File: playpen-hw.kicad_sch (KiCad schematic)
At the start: 2 parts, among them P1 USB_C_Plug_USB2.0, U1 STM32C011F6Px

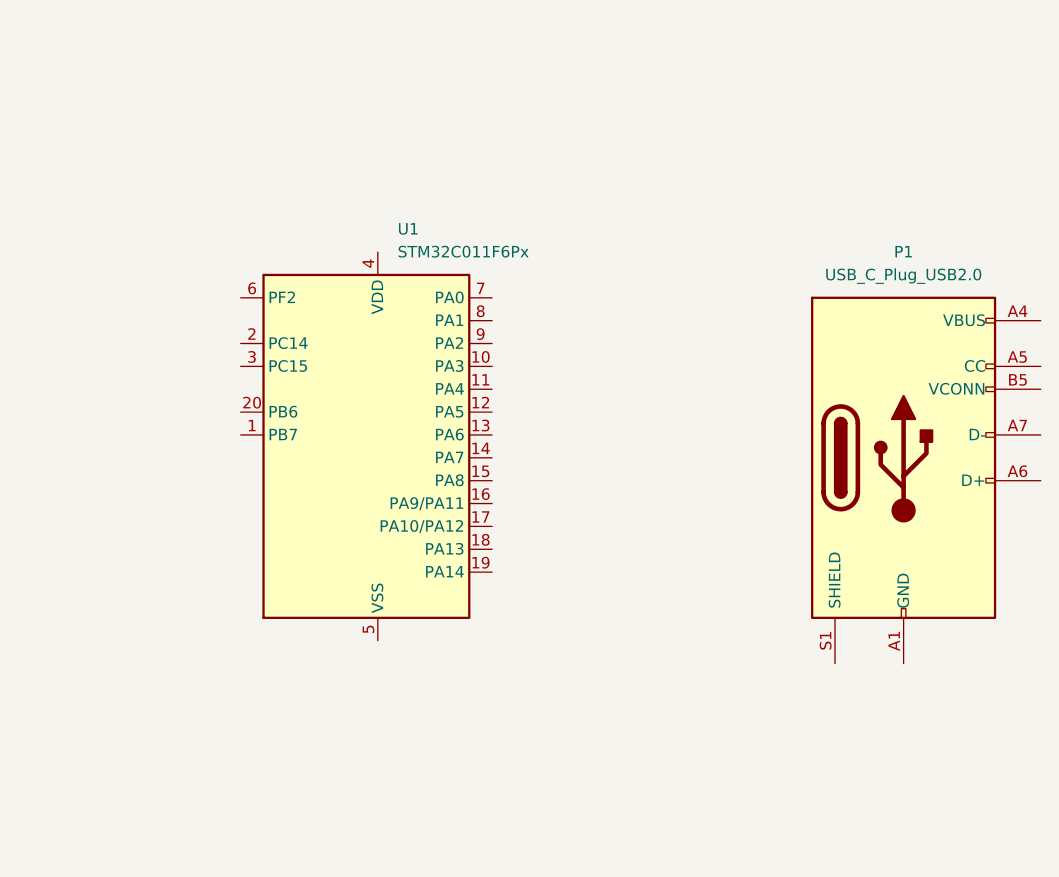
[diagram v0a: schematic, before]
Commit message: Changed to STM32 and gave a footprint to the USBC port
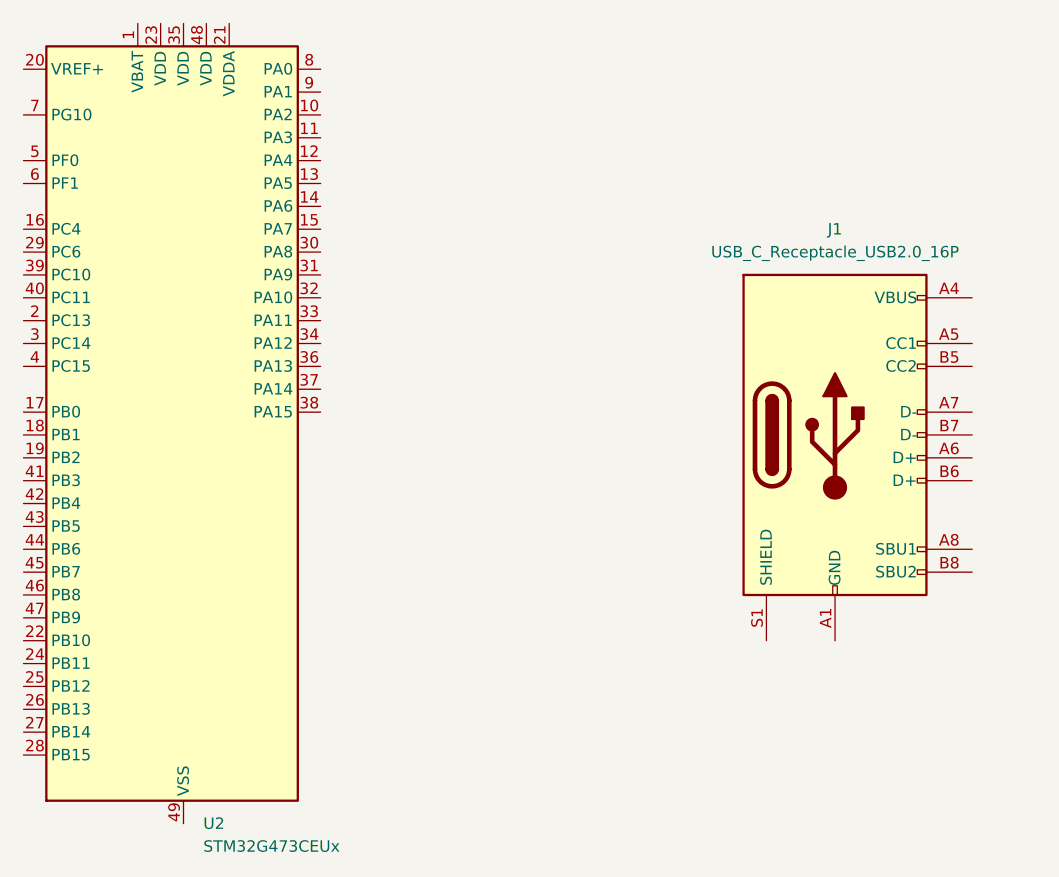
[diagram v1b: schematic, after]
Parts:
- removed P1: USB_C_Plug_USB2.0, symbol Connector:USB_C_Plug_USB2.0
- removed U1: STM32C011F6Px, Package_SO:TSSOP-20_4.4x6.5mm_P0.65mm, symbol MCU_ST_STM32C0:STM32C011F6Px
- added J1: USB_C_Receptacle_USB2.0_16P, Connector_USB:USB_C_Receptacle_GCT_USB4110, symbol Connector:USB_C_Receptacle_USB2.0_16P
- added U2: STM32G473CEUx, Package_DFN_QFN:QFN-48-1EP_7x7mm_P0.5mm_EP5.6x5.6mm, symbol MCU_ST_STM32G4:STM32G473CEUx
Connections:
- new net: J1.A1 (GND), J1.A12 (GND), J1.B1 (GND), J1.B12 (GND)
- new net: J1.A4 (VBUS), J1.A9 (VBUS), J1.B4 (VBUS), J1.B9 (VBUS)
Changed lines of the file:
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@@
 	(paper "A4")
 	(symbol
-		(lib_id "Connector:USB_C_Plug_USB2.0")
-		(at 166.37 95.25 0)
+		(lib_id "Connector:USB_C_Receptacle_USB2.0_16P")
+		(at 158.75 92.71 0)
 		(unit 1)
 		(exclude_from_sim no)
@@
 		(dnp no)
 		(fields_autoplaced yes)
-		(property "Reference" "P1"
-			(at 166.37 72.39 0)
-			(effects
-				(font
-					(size 1.27 1.27)
-				)
-			)
-		)
-		(property "Value" "USB_C_Plug_USB2.0"
-			(at 166.37 74.93 0)
-			(effects
-				(font
-					(size 1.27 1.27)
-				)
-			)
-		)
-		(property "Footprint" ""
-			(at 170.18 95.25 0)
+		(property "Reference" "J1"
+			(at 158.75 69.85 0)
+			(effects
+				(font
+					(size 1.27 1.27)
+				)
+			)
+		)
+		(property "Value" "USB_C_Receptacle_USB2.0_16P"
+			(at 158.75 72.39 0)
+			(effects
+				(font
+					(size 1.27 1.27)
+				)
+			)
+		)
+		(property "Footprint" "Connector_USB:USB_C_Receptacle_GCT_USB4110"
+			(at 162.56 92.71 0)
 			(effects
 				(font
@@
 		)
 		(property "Datasheet" "https://www.usb.org/sites/default/files/documents/usb_type-c.zip"
-			(at 170.18 95.25 0)
-			(effects
-				(font
-					(size 1.27 1.27)
-				)
-				(hide yes)
-			)
-		)
-		(property "Description" "USB 2.0-only Type-C Plug connector"
-			(at 166.37 95.25 0)
-			(effects
-				(font
-					(size 1.27 1.27)
-				)
-				(hide yes)
-			)
+			(at 162.56 92.71 0)
+			(effects
+				(font
+					(size 1.27 1.27)
+				)
+				(hide yes)
+			)
+		)
+		(property "Description" "USB 2.0-only 16P Type-C Receptacle connector"
+			(at 158.75 92.71 0)
+			(effects
+				(font
+					(size 1.27 1.27)
+				)
+				(hide yes)
+			)
+		)
+		(pin "A6"
+		)
+		(pin "S1"
 		)
 		(pin "B5"
 		)
-		(pin "S1"
+		(pin "B8"
+		)
+		(pin "B6"
+		)
+		(pin "A12"
+		)
+		(pin "A7"
+		)
+		(pin "A9"
+		)
+		(pin "B7"
+		)
+		(pin "A1"
+		)
+		(pin "B12"
+		)
+		(pin "B1"
+		)
+		(pin "B4"
+		)
+		(pin "B9"
 		)
 		(pin "A5"
 		)
-		(pin "A12"
-		)
-		(pin "A6"
-		)
-		(pin "A1"
-		)
-		(pin "A7"
-		)
-		(pin "A9"
-		)
-		(pin "B9"
-		)
-		(pin "B1"
+		(pin "A8"
 		)
 		(pin "A4"
-		)
-		(pin "B12"
-		)
-		(pin "B4"
 		)
 		(instances
 			(project ""
 				(path "/2d4792cf-ca90-482d-bff2-20a352af0b94"
-					(reference "P1")
+					(reference "J1")
 					(unit 1)
 				)
@@
 	)
 	(symbol
-		(lib_id "MCU_ST_STM32C0:STM32C011F6Px")
-		(at 105.41 95.25 0)
+		(lib_id "MCU_ST_STM32G4:STM32G473CEUx")
+		(at 83.82 92.71 0)
 		(unit 1)
 		(exclude_from_sim no)
@@
 		(dnp no)
 		(fields_autoplaced yes)
-		(property "Reference" "U1"
-			(at 110.1441 69.85 0)
+		(property "Reference" "U2"
+			(at 88.5541 135.89 0)
 			(effects
 				(font
@@
 			)
 		)
-		(property "Value" "STM32C011F6Px"
-			(at 110.1441 72.39 0)
+		(property "Value" "STM32G473CEUx"
+			(at 88.5541 138.43 0)
 			(effects
 				(font
@@
 			)
 		)
-		(property "Footprint" "Package_SO:TSSOP-20_4.4x6.5mm_P0.65mm"
-			(at 95.25 113.03 0)
+		(property "Footprint" "Package_DFN_QFN:QFN-48-1EP_7x7mm_P0.5mm_EP5.6x5.6mm"
+			(at 71.12 133.35 0)
 			(effects
 				(font
@@
 			)
 		)
-		(property "Datasheet" "https://www.st.com/resource/en/datasheet/stm32c011f6.pdf"
-			(at 105.41 95.25 0)
-			(effects
-				(font
-					(size 1.27 1.27)
-				)
-				(hide yes)
-			)
-		)
-		(property "Description" "STMicroelectronics Arm Cortex-M0+ MCU, 32KB flash, 6KB RAM, 48 MHz, 2.0-3.6V, 18 GPIO, TSSOP20"
-			(at 105.41 95.25 0)
-			(effects
-				(font
-					(size 1.27 1.27)
-				)
-				(hide yes)
-			)
+		(property "Datasheet" "https://www.st.com/resource/en/datasheet/stm32g473ce.pdf"
+			(at 83.82 92.71 0)
+			(effects
+				(font
+					(size 1.27 1.27)
+				)
+				(hide yes)
+			)
+		)
+		(property "Description" "STMicroelectronics Arm Cortex-M4 MCU, 512KB flash, 128KB RAM, 170 MHz, 1.71-3.6V, 42 GPIO, UFQFPN48"
+			(at 83.82 92.71 0)
+			(effects
+				(font
+					(size 1.27 1.27)
+				)
+				(hide yes)
+			)
+		)
+		(pin "27"
+		)
+		(pin "25"
+		)
+		(pin "8"
+		)
+		(pin "49"
+		)
+		(pin "29"
+		)
+		(pin "3"
+		)
+		(pin "11"
+		)
+		(pin "40"
+		)
+		(pin "23"
+		)
+		(pin "22"
+		)
+		(pin "38"
+		)
+		(pin "48"
+		)
+		(pin "5"
+		)
+		(pin "10"
+		)
+		(pin "36"
+		)
+		(pin "37"
+		)
+		(pin "15"
 		)
 		(pin "16"
 		)
+		(pin "32"
+		)
+		(pin "33"
+		)
+		(pin "1"
+		)
+		(pin "39"
+		)
+		(pin "31"
+		)
+		(pin "43"
+		)
+		(pin "12"
+		)
+		(pin "17"
+		)
+		(pin "19"
+		)
+		(pin "26"
+		)
+		(pin "35"
+		)
+		(pin "20"
+		)
+		(pin "30"
+		)
+		(pin "44"
+		)
+		(pin "21"
+		)
+		(pin "2"
+		)
+		(pin "28"
+		)
+		(pin "4"
+		)
+		(pin "45"
+		)
+		(pin "46"
+		)
+		(pin "6"
+		)
+		(pin "7"
+		)
+		(pin "13"
+		)
 		(pin "14"
 		)
-		(pin "6"
-		)
-		(pin "5"
-		)
-		(pin "13"
-		)
-		(pin "20"
-		)
-		(pin "15"
-		)
-		(pin "3"
-		)
-		(pin "4"
-		)
-		(pin "10"
-		)
 		(pin "18"
 		)
-		(pin "11"
-		)
-		(pin "2"
-		)
-		(pin "8"
-		)
-		(pin "12"
-		)
-		(pin "1"
-		)
-		(pin "19"
-		)
-		(pin "17"
+		(pin "24"
+		)
+		(pin "34"
+		)
+		(pin "42"
+		)
+		(pin "41"
+		)
+		(pin "47"
 		)
 		(pin "9"
-		)
-		(pin "7"
 		)
 		(instances
 			(project ""
 				(path "/2d4792cf-ca90-482d-bff2-20a352af0b94"
-					(reference "U1")
+					(reference "U2")
 					(unit 1)
 				)

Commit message: Testing KiCAD CI job (#2)
* Testing KiCAD CI job

* Splitting into multiple workflows for scalability

* Naming workflows better names
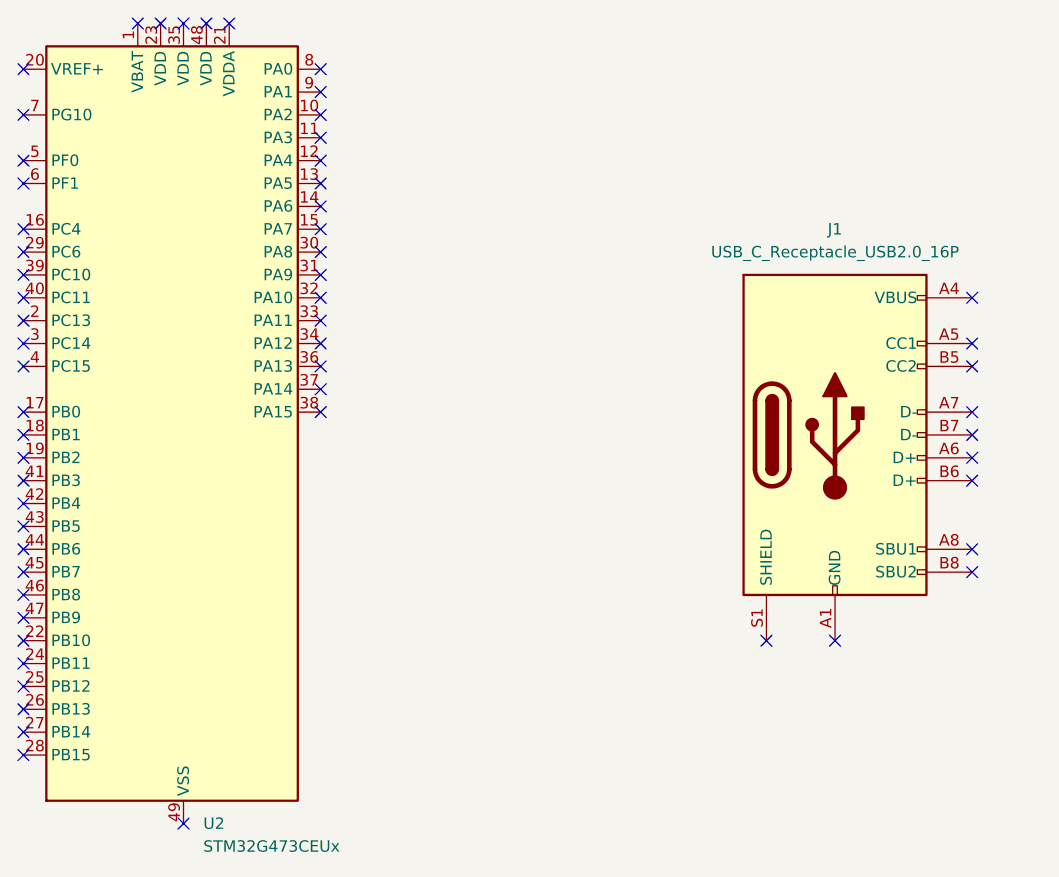
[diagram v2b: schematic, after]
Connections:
- no-connect marks 0 -> 60
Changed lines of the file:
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@@
 	(generator_version "8.0")
 	(paper "A4")
+	(no_connect
+		(at 101.6 80.01)
+	)
+	(no_connect
+		(at 101.6 52.07)
+	)
+	(no_connect
+		(at 101.6 90.17)
+	)
+	(no_connect
+		(at 173.99 82.55)
+	)
+	(no_connect
+		(at 68.58 125.73)
+	)
+	(no_connect
+		(at 68.58 123.19)
+	)
+	(no_connect
+		(at 68.58 115.57)
+	)
+	(no_connect
+		(at 68.58 92.71)
+	)
+	(no_connect
+		(at 151.13 115.57)
+	)
+	(no_connect
+		(at 68.58 100.33)
+	)
+	(no_connect
+		(at 91.44 46.99)
+	)
+	(no_connect
+		(at 68.58 110.49)
+	)
+	(no_connect
+		(at 68.58 77.47)
+	)
+	(no_connect
+		(at 173.99 95.25)
+	)
+	(no_connect
+		(at 173.99 77.47)
+	)
+	(no_connect
+		(at 68.58 85.09)
+	)
+	(no_connect
+		(at 173.99 97.79)
+	)
+	(no_connect
+		(at 68.58 57.15)
+	)
+	(no_connect
+		(at 68.58 52.07)
+	)
+	(no_connect
+		(at 101.6 72.39)
+	)
+	(no_connect
+		(at 101.6 62.23)
+	)
+	(no_connect
+		(at 68.58 74.93)
+	)
+	(no_connect
+		(at 86.36 135.89)
+	)
+	(no_connect
+		(at 68.58 90.17)
+	)
+	(no_connect
+		(at 173.99 92.71)
+	)
+	(no_connect
+		(at 86.36 46.99)
+	)
+	(no_connect
+		(at 81.28 46.99)
+	)
+	(no_connect
+		(at 68.58 82.55)
+	)
+	(no_connect
+		(at 68.58 64.77)
+	)
+	(no_connect
+		(at 68.58 95.25)
+	)
+	(no_connect
+		(at 101.6 67.31)
+	)
+	(no_connect
+		(at 173.99 107.95)
+	)
+	(no_connect
+		(at 68.58 62.23)
+	)
+	(no_connect
+		(at 101.6 64.77)
+	)
+	(no_connect
+		(at 173.99 105.41)
+	)
+	(no_connect
+		(at 173.99 85.09)
+	)
+	(no_connect
+		(at 68.58 69.85)
+	)
+	(no_connect
+		(at 68.58 128.27)
+	)
+	(no_connect
+		(at 68.58 72.39)
+	)
+	(no_connect
+		(at 68.58 107.95)
+	)
+	(no_connect
+		(at 88.9 46.99)
+	)
+	(no_connect
+		(at 101.6 87.63)
+	)
+	(no_connect
+		(at 101.6 82.55)
+	)
+	(no_connect
+		(at 101.6 69.85)
+	)
+	(no_connect
+		(at 83.82 46.99)
+	)
+	(no_connect
+		(at 68.58 80.01)
+	)
+	(no_connect
+		(at 101.6 57.15)
+	)
+	(no_connect
+		(at 101.6 59.69)
+	)
+	(no_connect
+		(at 68.58 113.03)
+	)
+	(no_connect
+		(at 158.75 115.57)
+	)
+	(no_connect
+		(at 101.6 77.47)
+	)
+	(no_connect
+		(at 173.99 90.17)
+	)
+	(no_connect
+		(at 68.58 105.41)
+	)
+	(no_connect
+		(at 101.6 54.61)
+	)
+	(no_connect
+		(at 68.58 102.87)
+	)
+	(no_connect
+		(at 68.58 120.65)
+	)
+	(no_connect
+		(at 68.58 118.11)
+	)
+	(no_connect
+		(at 101.6 74.93)
+	)
+	(no_connect
+		(at 101.6 85.09)
+	)
+	(no_connect
+		(at 68.58 97.79)
+	)
 	(symbol
 		(lib_id "Connector:USB_C_Receptacle_USB2.0_16P")
